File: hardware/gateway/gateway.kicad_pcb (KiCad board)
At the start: 2 copper layers, 100 x 45 mm, 79 parts, among them IC1 STM8L151K4T6, IC2 CC1101RGPR, IC3 LT1615ES5-1#TRMPBF, IC4 MIC4427YM, IC5 MB85RC64TAPNF-G-BDERE1, J1 G8250041000YEU, J2 M20-9770342, Q1 IRLML6402TRPBF, U1 2462, Y1 NX3225GA-26.000M-STD-CRG-2

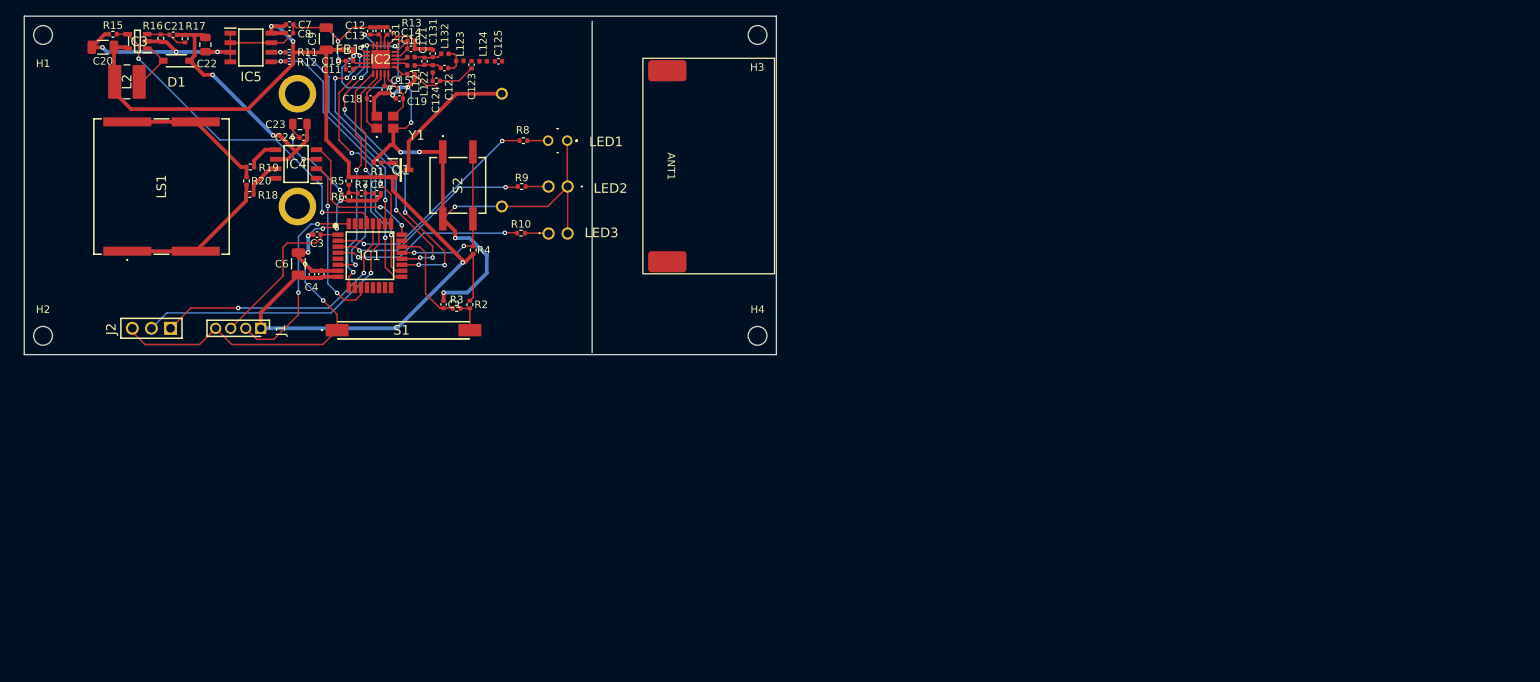
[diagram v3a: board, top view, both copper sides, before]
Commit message: EG-12 GND disconnected and ground plane created. Still changes to be done on power lines and GND.
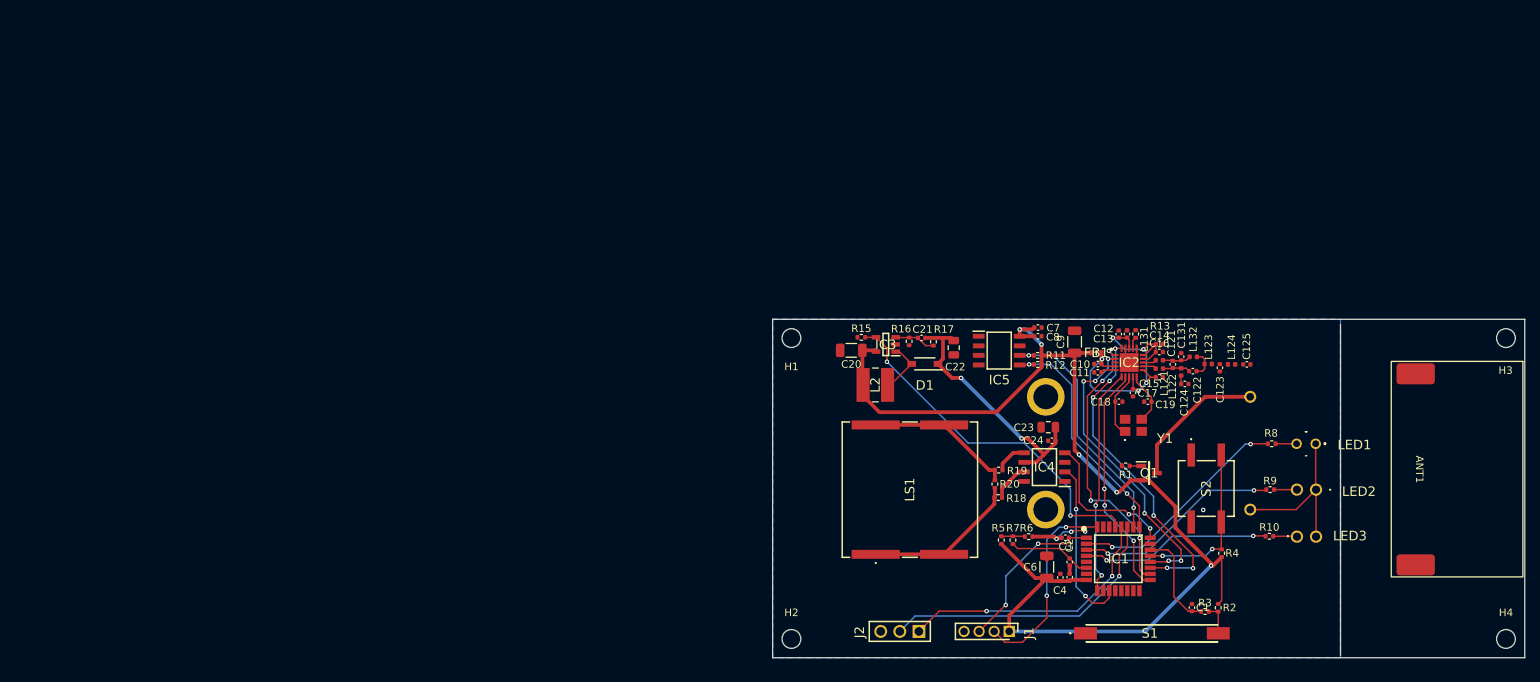
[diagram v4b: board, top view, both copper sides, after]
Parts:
- moved ANT1 107.4 mm to (265.0, 134.9)
- moved C123 107.4 mm to (239.0, 121.4)
- moved C15 107.4 mm to (230.9, 122.7)
- moved C18 107.4 mm to (225.5, 125.9)
- moved C19 107.4 mm to (229.4, 125.9)
- moved C23 107.4 mm to (216.2, 129.3)
- moved C4 107.4 mm to (217.8, 149.3)
- moved C5 107.4 mm to (219.0, 149.2)
- moved FB1 107.4 mm to (222.5, 119.4)
- moved L123 107.4 mm to (237.4, 120.9)
- moved L131 107.4 mm to (230.9, 120.4)
- moved L2 107.4 mm to (193.2, 123.7)
- moved Q1 107.4 mm to (229.6, 135.4)
- moved R10 107.4 mm to (245.5, 143.8)
- moved R13 107.4 mm to (227.8, 116.9)
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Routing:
- net GND: track 257.3 -> 38.6 mm, vias 23 -> 4
- net VDD: track 147.5 -> 156.5 mm, vias 3 -> 5
- net V_MEAS: track 15.9 -> 11.1 mm, vias 2 -> 0
- net Net-(R5-Pad1): track 2.28 -> 3.16 mm
- net /MCU/SCLK: track 36.8 -> 37.6 mm
- net /MCU/IRQ: track 31.1 -> 30.5 mm
- net /MCU/CS: track 30.7 -> 31.2 mm, vias 2 -> 3
- net NRST: vias 0 -> 2
- added copper zone on B.Cu, net GND

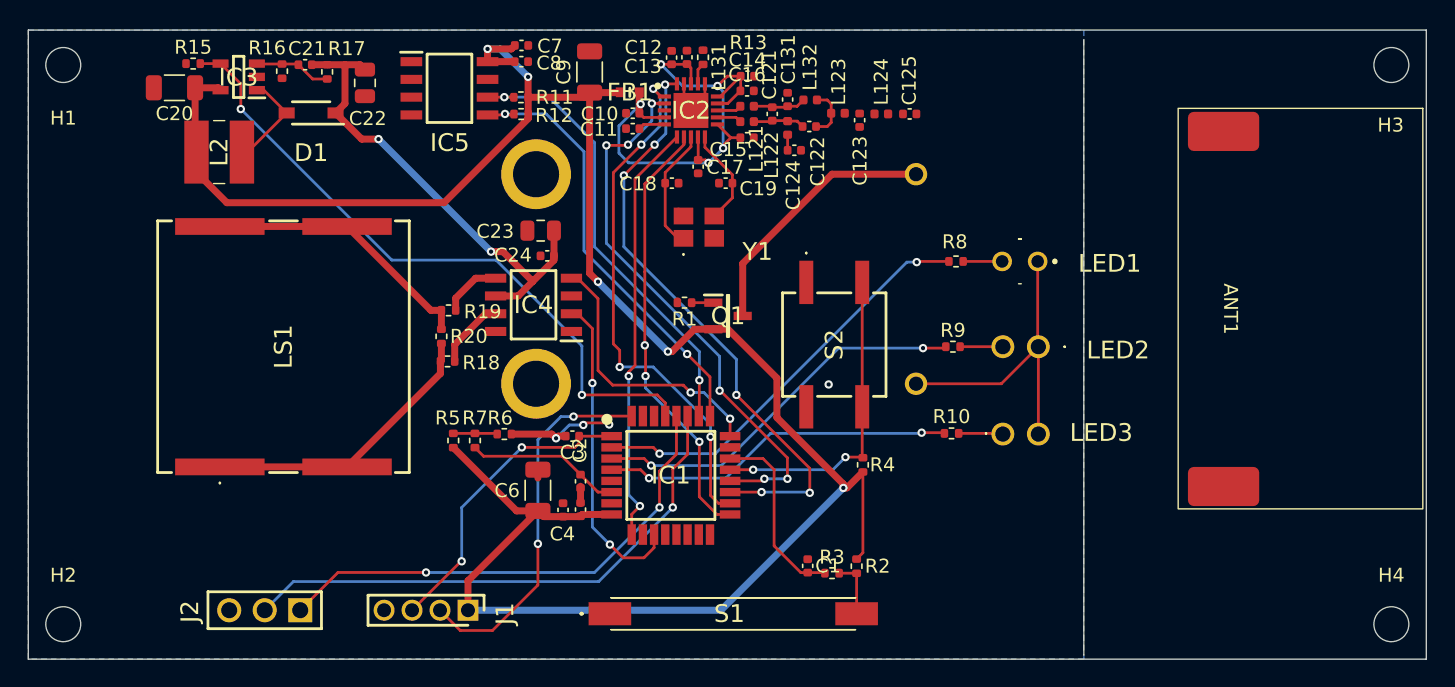
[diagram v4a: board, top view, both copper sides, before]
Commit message: EG-12 Fixes on SPI signals and ground planes. Antenna connected with Coplanar wavelenght. Only missing vias to connect grounds and run the DRC.
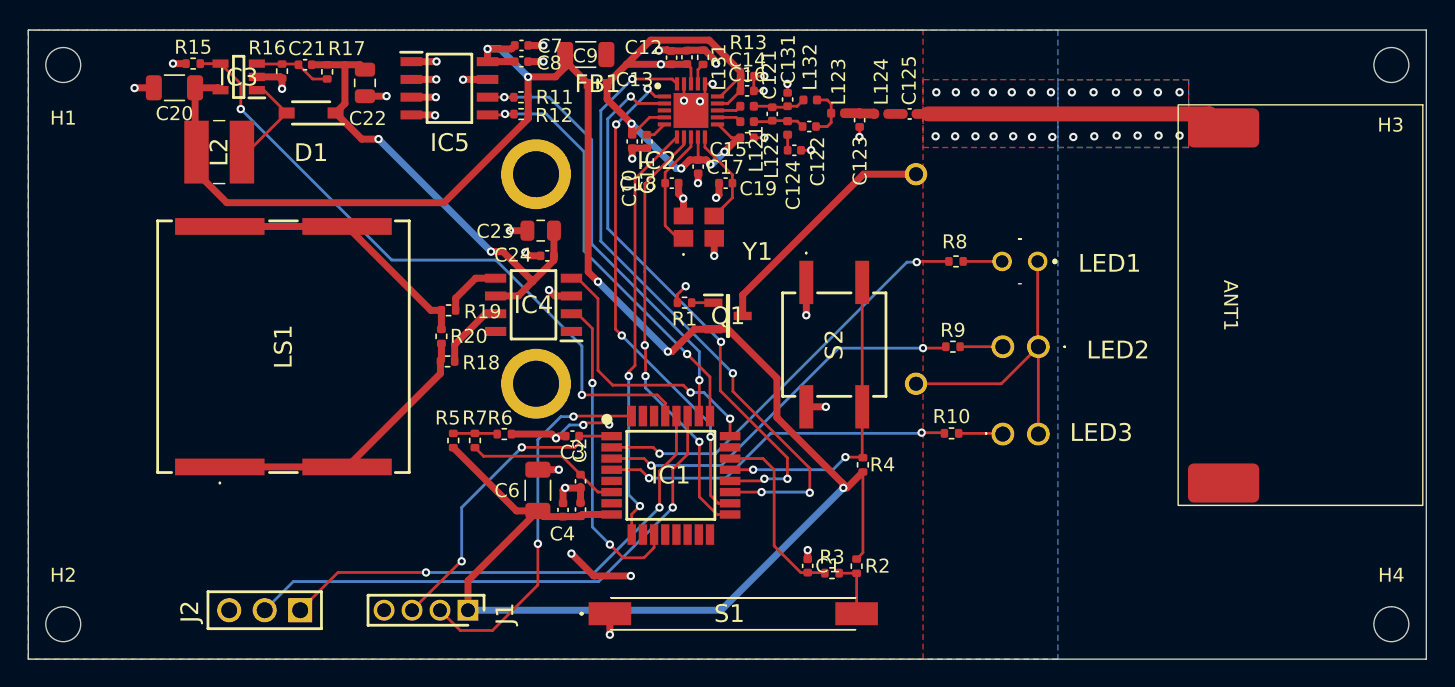
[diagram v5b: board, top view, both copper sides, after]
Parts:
- moved FB1 2.38 mm to (220.2, 118.8)
- moved C10 2.02 mm to (222.7, 122.9), turned to -90 degrees
- moved C11 1.37 mm to (223.8, 122.9), turned to -90 degrees
- moved C9 1.28 mm to (219.4, 116.7), turned to 0 degrees
- moved ANT1 0.25 mm to (265.0, 134.7)
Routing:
- net GND: track 38.6 -> 93.6 mm, vias 4 -> 68
- net /RF/RF_LINE: track 0.00 -> 22.4 mm
- net RF_VDD: track 41.2 -> 44.5 mm
- net /MCU/SDI: track 42.6 -> 45.8 mm, vias 6 -> 4
- net Net-(C123-Pad2): track 0.07 -> 2.15 mm
- net /MCU/SCLK: track 37.6 -> 36.0 mm
- net BAT_IN: track 18.9 -> 17.5 mm
- net Net-(C125-Pad1): track 0.00 -> 1.06 mm
- net /MCU/SDO: track 39.5 -> 40.2 mm, vias 6 -> 4
- net VDD: track 156.5 -> 157.0 mm
- added copper zone on F.Cu, net GND
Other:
- outline, holes or cut-outs redrawn

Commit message: EG-12 All DRC erros and warnings fixed. Only missing the vias connecting the ground planes.
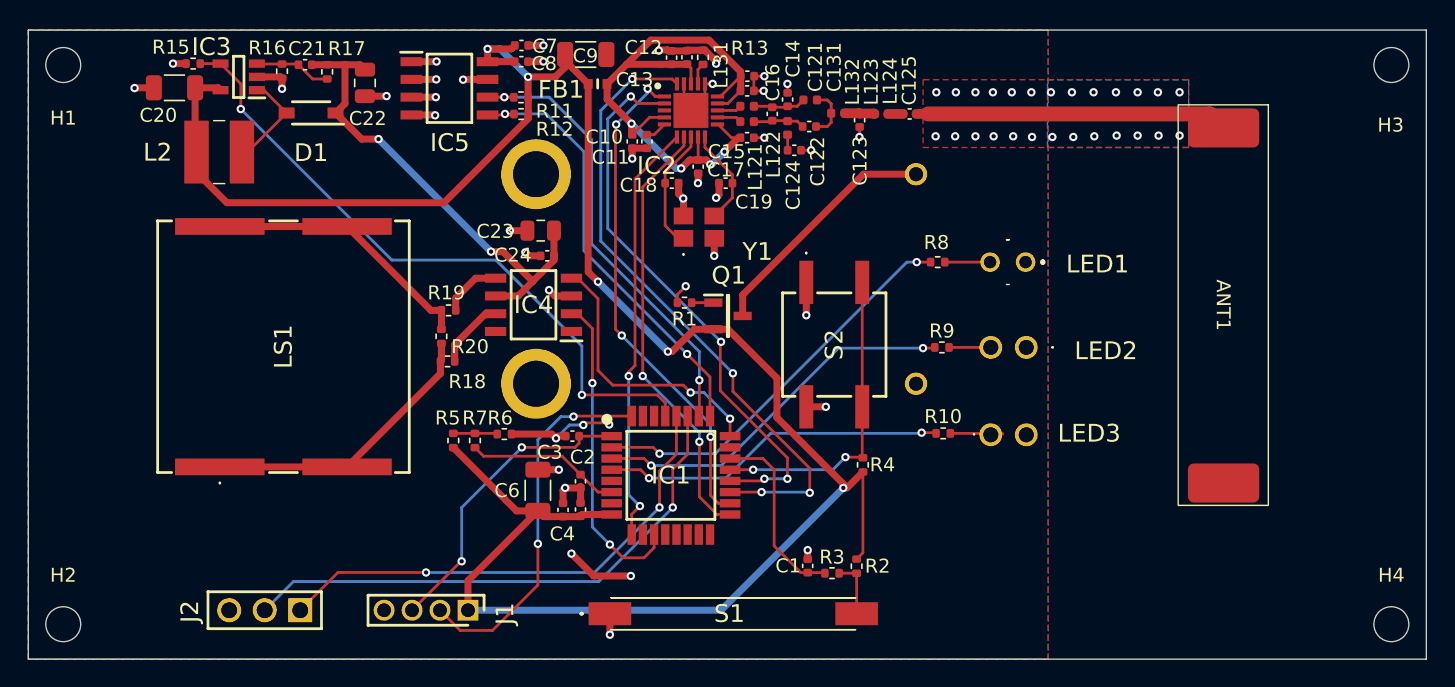
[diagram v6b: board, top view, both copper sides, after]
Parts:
- moved R8 1.31 mm to (244.6, 131.6)
- moved LED3 0.86 mm to (248.3, 143.9)
- moved LED1 0.86 mm to (250.8, 131.6)
- moved LED2 0.86 mm to (250.9, 137.7)
- moved R9 0.79 mm to (244.8, 137.7)
- moved R10 0.60 mm to (244.9, 143.8)
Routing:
- net GND: track 93.6 -> 71.4 mm, vias 68 -> 66
- net LED_B: track 30.0 -> 28.7 mm
- net LED_Y: track 27.6 -> 26.8 mm
- net LED_R: track 25.4 -> 24.8 mm
- net /MCU/CS: track 31.2 -> 31.4 mm, vias 3 -> 2
- net RF_VDD: vias 5 -> 4

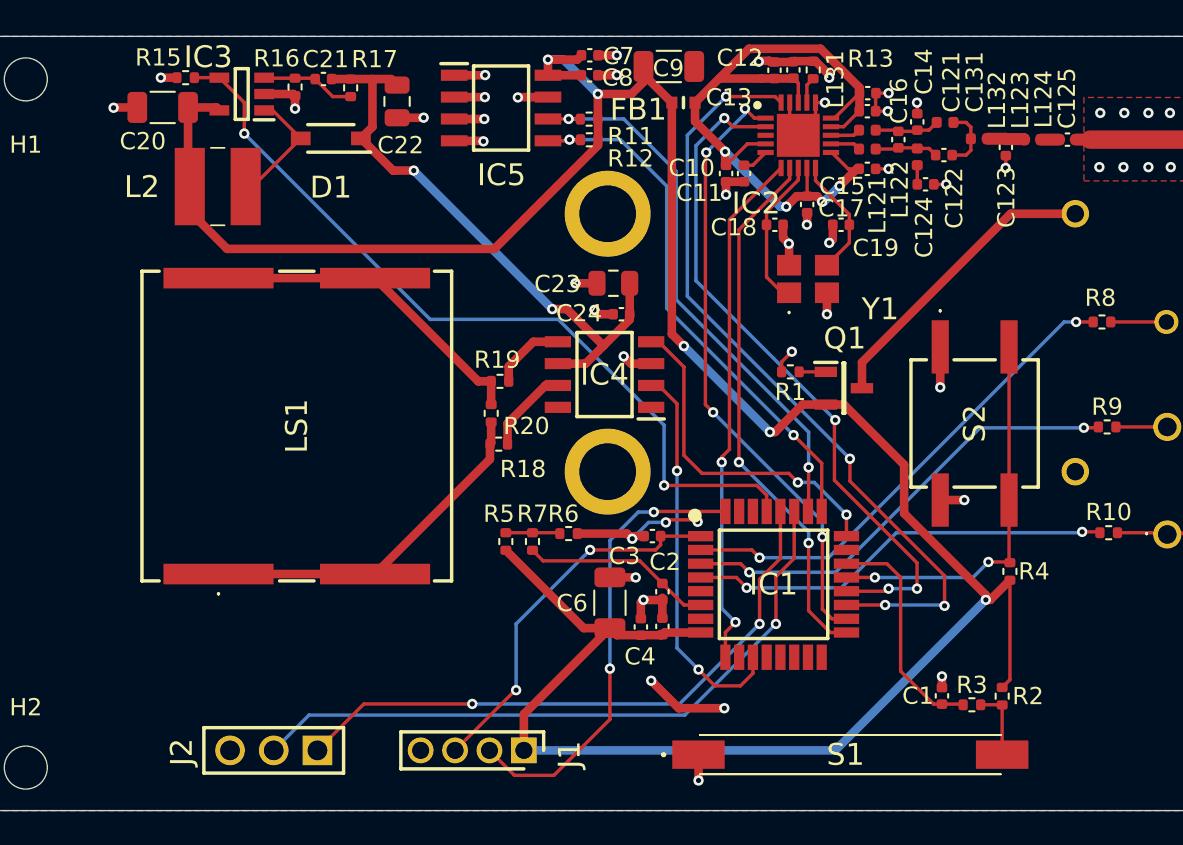
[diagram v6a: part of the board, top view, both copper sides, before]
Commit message: EG-12 Vias inserted to connecvt both ground planes (top and bottom). No DRC errors. All done.
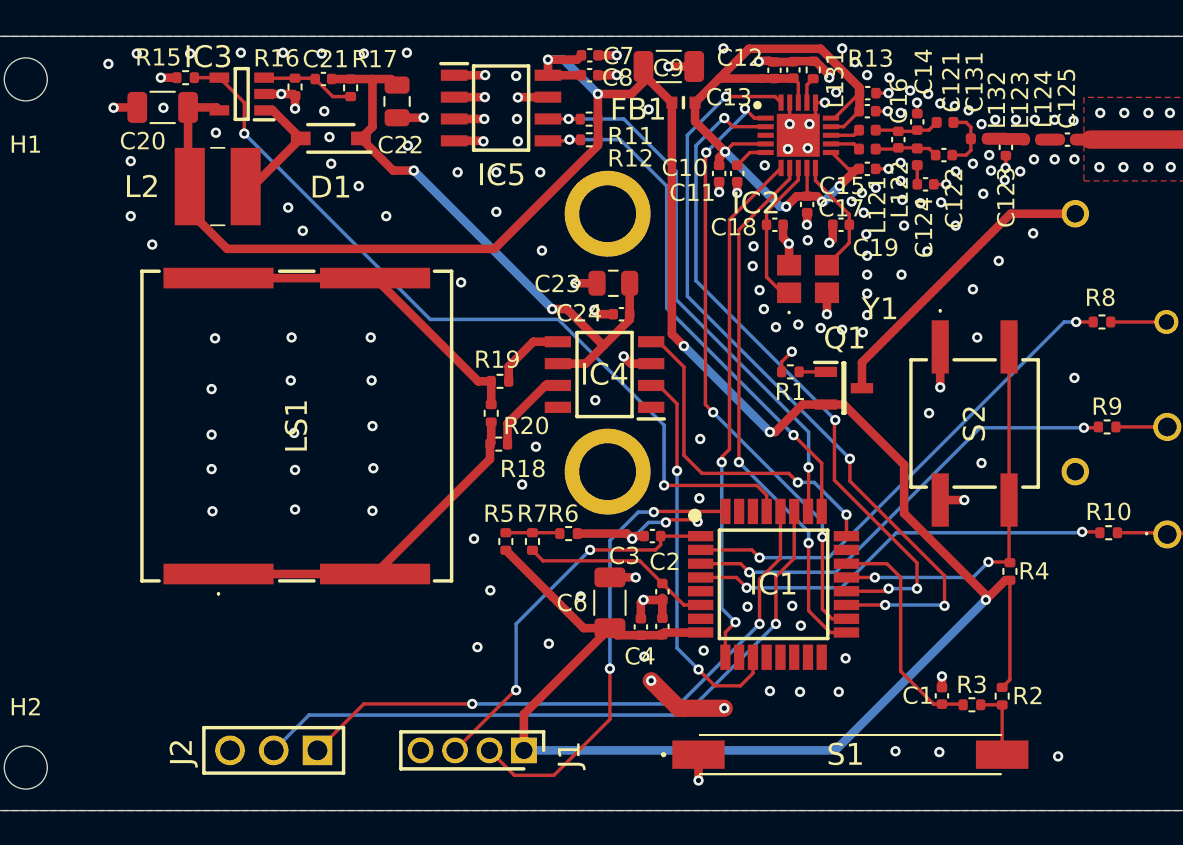
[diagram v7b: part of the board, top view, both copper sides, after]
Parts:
- moved C11 0.40 mm to (223.3, 122.9)
- moved C10 0.40 mm to (222.3, 122.9)
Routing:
- net GND: track 71.4 -> 73.4 mm, vias 66 -> 205
